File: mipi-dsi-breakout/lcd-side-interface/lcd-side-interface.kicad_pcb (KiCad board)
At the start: 2 copper layers, 8 parts

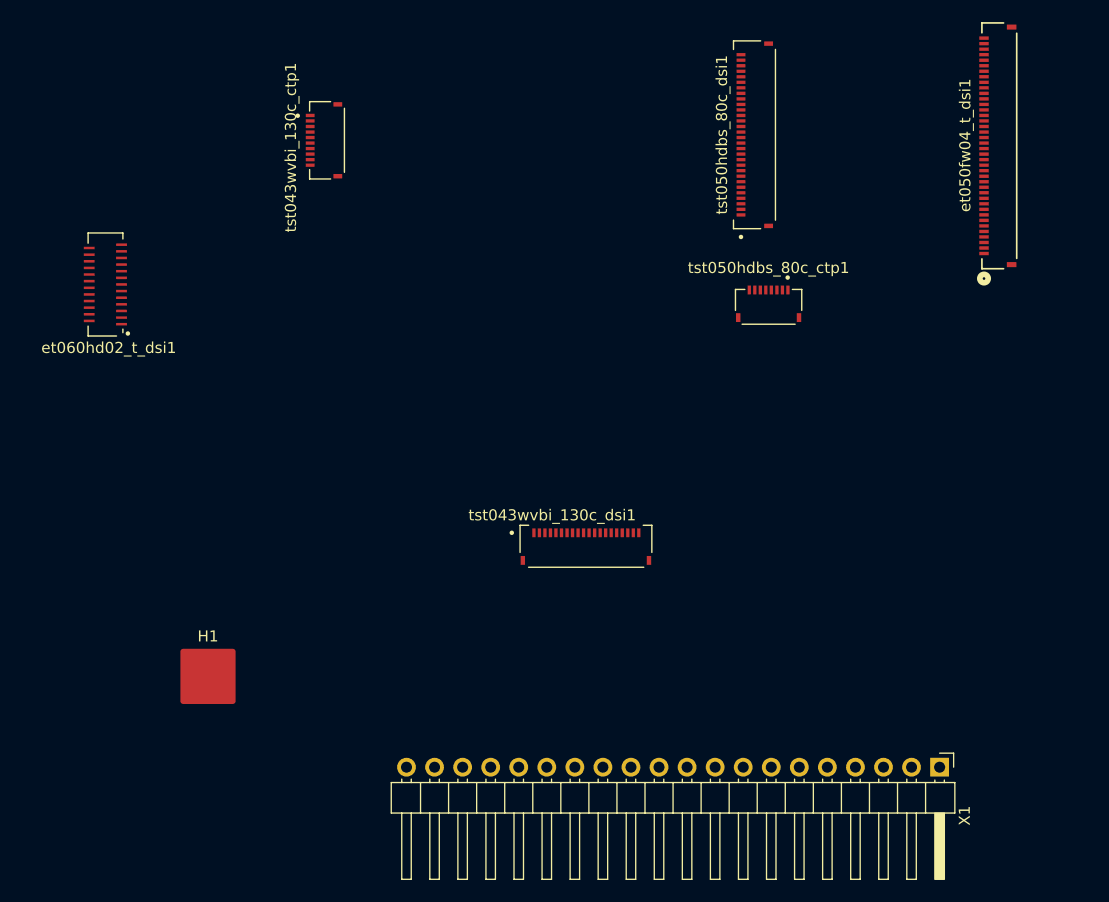
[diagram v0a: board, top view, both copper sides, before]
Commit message: Fill out lcd side interface + double check errors.
* Flip orientation of most connectors to match orientation of real world
  parts.

* Added NC pins to symbol so they are matched up to the footprints.

* Added a RESET_FAILSAFE solder bridge that can be cut in the case that
  the CTP touch screen resets aren't active low and the DSI resets are.

* Double check pin ordering and reset signals.
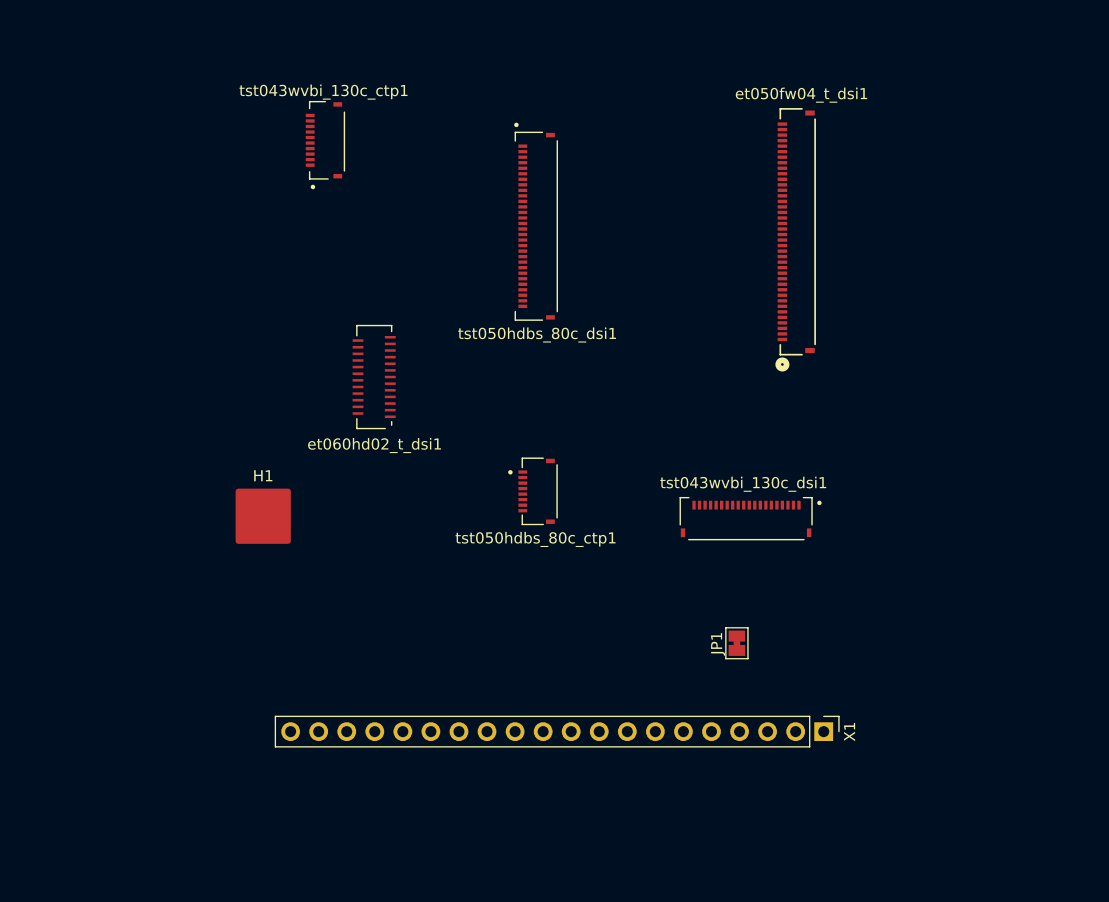
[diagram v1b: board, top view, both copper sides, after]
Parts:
- added JP1: SolderJumper_2_Bridged, Jumper:SolderJumper-2_P1.3mm_Bridged_Pad1.0x1.5mm, F.Cu at (153.9, 113.0)
- X1: footprint Connector_PinHeader_2.54mm:PinHeader_1x20_P2.54mm_Horizontal -> Connector_PinHeader_2.54mm:PinHeader_1x20_P2.54mm_Vertical
- moved tst050hdbs_80c_ctp1 27.1 mm to (135.7, 99.2), turned to 90 degrees
- moved et060hd02_t_dsi1 25.7 mm to (121.1, 89.2)
- moved tst050hdbs_80c_dsi1 21.4 mm to (135.7, 75.2)
- moved et050fw04_t_dsi1 19.8 mm to (158.0, 85.5)
- moved H1 15.3 mm to (111.0, 101.5)
- moved tst043wvbi_130c_dsi1 14.7 mm to (157.2, 101.7)
- moved X1 11.0 mm to (161.7, 121.0)
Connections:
- et050fw04_t_dsi1 pad 11: (no net) -> unconnected-(et050fw04_t_dsi1-NC-Pad11)
- et050fw04_t_dsi1 pad 12: (no net) -> unconnected-(et050fw04_t_dsi1-NC-Pad12)
- et050fw04_t_dsi1 pad 14: (no net) -> unconnected-(et050fw04_t_dsi1-NC-Pad14)
- et050fw04_t_dsi1 pad 15: (no net) -> unconnected-(et050fw04_t_dsi1-NC-Pad15)
- et050fw04_t_dsi1 pad 21: (no net) -> unconnected-(et050fw04_t_dsi1-NC-Pad21)
- et050fw04_t_dsi1 pad 23: (no net) -> unconnected-(et050fw04_t_dsi1-NC-Pad23)
- et050fw04_t_dsi1 pad 25: (no net) -> unconnected-(et050fw04_t_dsi1-NC-Pad25)
- et050fw04_t_dsi1 pad 26: (no net) -> unconnected-(et050fw04_t_dsi1-NC-Pad26)
- et050fw04_t_dsi1 pad 31: (no net) -> unconnected-(et050fw04_t_dsi1-NC-Pad31)
- et050fw04_t_dsi1 pad 34: (no net) -> unconnected-(et050fw04_t_dsi1-NC-Pad34)
- et050fw04_t_dsi1 pad 40: (no net) -> unconnected-(et050fw04_t_dsi1-NC-Pad40)
- et060hd02_t_dsi1 pad 20: (no net) -> unconnected-(et060hd02_t_dsi1-NC-Pad20)
- et060hd02_t_dsi1 pad 23: (no net) -> unconnected-(et060hd02_t_dsi1-NC-Pad23)
- tst043wvbi_130c_ctp1 pad 1: (no net) -> unconnected-(tst043wvbi_130c_ctp1-NC-Pad1)
- tst043wvbi_130c_ctp1 pad 2: (no net) -> unconnected-(tst043wvbi_130c_ctp1-NC-Pad2)
- tst043wvbi_130c_ctp1 pad 3: /RESET -> /RESET_FAILSAFE
- tst043wvbi_130c_dsi1 pad 20: (no net) -> GND
- tst050hdbs_80c_ctp1 pad 7: /RESET -> /RESET_FAILSAFE
- tst050hdbs_80c_dsi1 pad 1: (no net) -> unconnected-(tst050hdbs_80c_dsi1-NC-Pad1)
- tst050hdbs_80c_dsi1 pad 29: (no net) -> unconnected-(tst050hdbs_80c_dsi1-NC-Pad29)
- tst050hdbs_80c_dsi1 pad 30: (no net) -> unconnected-(tst050hdbs_80c_dsi1-NC-Pad30)
- tst050hdbs_80c_dsi1 pad 9: (no net) -> unconnected-(tst050hdbs_80c_dsi1-NC-Pad9)

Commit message: Do first pass of positioning for zif connectors.
In mipi dsi lcd side interface board. Need to double check measurements
again, just to be sure.
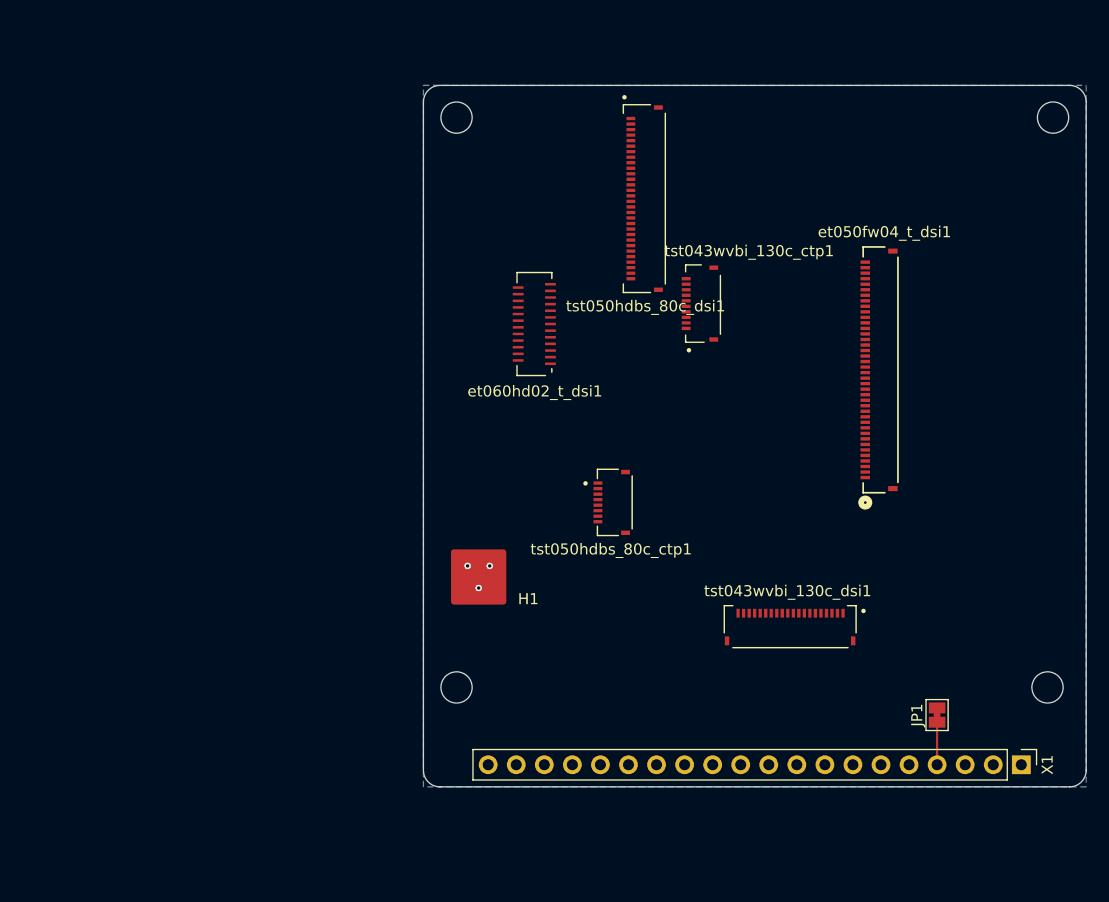
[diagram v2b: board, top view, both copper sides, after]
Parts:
- moved tst043wvbi_130c_ctp1 37.1 mm to (149.3, 80.0)
- moved H1 20.3 mm to (130.5, 107.0)
- moved JP1 19.3 mm to (172.0, 119.5)
- moved X1 18.1 mm to (179.6, 124.0)
- moved et060hd02_t_dsi1 15.3 mm to (135.6, 84.4)
- moved et050fw04_t_dsi1 14.6 mm to (165.5, 98.0)
- moved tst043wvbi_130c_dsi1 10.6 mm to (161.2, 111.5)
- moved tst050hdbs_80c_dsi1 10.1 mm to (145.5, 72.8)
- moved tst050hdbs_80c_ctp1 6.87 mm to (142.5, 100.2)
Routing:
- net /RESET: track 0.00 -> 3.85 mm
- net GND: vias 0 -> 3
- added copper zone on B.Cu, net GND
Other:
- board outline added: 60 x 63.5 mm
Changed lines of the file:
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@@
 	(footprint "Jumper:SolderJumper-2_P1.3mm_Bridged_Pad1.0x1.5mm"
 		(layer "F.Cu")
-		(at 153.88 113 90)
+		(at 172 119.5 90)
 		(descr "SMD Solder Jumper, 1x1.5mm Pads, 0.3mm gap, bridged with 1 copper strip")
 		(tags "net tie solder jumper bridged")
@@
 		)
 		(property "Value" "SolderJumper_2_Bridged"
-			(at 0 1.9 90)
+			(at 2.5 -0.3 0)
 			(layer "F.Fab")
 			(effects
@@
 	(footprint "project:sus-grounding-pad"
 		(layer "F.Cu")
-		(at 111 101.5)
+		(at 130.5 107)
 		(property "Reference" "H1"
-			(at 0 -3.625 0)
+			(at 4.5 2 0)
 			(unlocked yes)
 			(layer "F.SilkS")
@@
 		)
 		(property "Value" "MountingHole_Pad"
-			(at 0 3.625 0)
+			(at 0 4 0)
 			(unlocked yes)
 			(layer "F.Fab")
@@
 		)
 		(fp_text user "${REFERENCE}"
-			(at 0 5.625 0)
+			(at 4.5 2 0)
 			(unlocked yes)
 			(layer "F.Fab")
@@
 	(footprint "project:Cvilux_CF4240FH0R0-05-NH_40pos-0.5mm-zif"
 		(layer "F.Cu")
-		(at 158 85.500002 90)
+		(at 165.499878 98.000001 90)
 		(tags "CF4240FH0R0-05-NH ")
 		(property "Reference" "et050fw04_t_dsi1"
@@
 	(footprint "Connector_PinHeader_2.54mm:PinHeader_1x20_P2.54mm_Vertical"
 		(layer "F.Cu")
-		(at 161.74 121 -90)
+		(at 179.625 124 -90)
 		(descr "Through hole straight pin header, 1x20, 2.54mm pitch, single row")
 		(tags "Through hole pin header THT 1x20 2.54mm single row")
@@
 	(footprint "project:TE_2328702_8pos-0.5mm-zif"
 		(layer "F.Cu")
-		(at 135.7 99.25 90)
+		(at 142.5 100.25 90)
 		(property "Reference" "tst050hdbs_80c_ctp1"
 			(at -4.25 0 180)
@@
 	(footprint "project:Cvilux_CF4230FH0R0-05-NH_30pos-0.5mm-zif"
 		(layer "F.Cu")
-		(at 135.72 75.25 90)
+		(at 145.5 72.75 90)
 		(property "Reference" "tst050hdbs_80c_dsi1"
 			(at -9.741929 0.11858 0)
@@
 	(footprint "project:Cvilux_CF5825DH0RA-NH_25pos-0.3mm-zif"
 		(layer "F.Cu")
-		(at 121.1 89.19 90)
+		(at 135.6 84.39 90)
 		(property "Reference" "et060hd02_t_dsi1"
 			(at -5.81 0 0)
@@
 	(footprint "project:Cvilux_CF4220FH0R0-05-NH_20pos-0.5mm-zif"
 		(layer "F.Cu")
-		(at 157.25 101.72)
+		(at 161.2375 111.5)
 		(property "Reference" "tst043wvbi_130c_dsi1"
 			(at -2.75 -3.22 0)
@@
 	(footprint "project:TE_1-2328702-0_10pos-0.5mm-zif"
 		(layer "F.Cu")
-		(at 115.25 65.22 90)
+		(at 149.2875 80 90)
 		(property "Reference" "tst043wvbi_130c_ctp1"
-			(at 2.22 1.25 180)
+			(at 2.5 5.7125 180)
 			(layer "F.SilkS")
 			(effects
@@
 			)
 		)
+	)
+	(gr_line
+		(start 185.5 124.5)
+		(end 185.5 64)
+		(stroke
+			(width 0.05)
+			(type default)
+		)
+		(layer "Edge.Cuts")
+	)
+	(gr_circle
+		(center 182 117)
+		(end 183 118)
+		(stroke
+			(width 0.05)
+			(type default)
+		)
+		(fill no)
+		(layer "Edge.Cuts")
+	)
+	(gr_arc
+		(start 125.5 64)
+		(mid 125.93934 62.93934)
+		(end 127 62.5)
+		(stroke
+			(width 0.05)
+			(type default)
+		)
+		(layer "Edge.Cuts")
+	)
+	(gr_circle
+		(center 128.5 65.414214)
+		(end 129.5 66.414214)
+		(stroke
+			(width 0.05)
+			(type default)
+		)
+		(fill no)
+		(layer "Edge.Cuts")
+	)
+	(gr_line
+		(start 184 62.5)
+		(end 127 62.5)
+		(stroke
+			(width 0.05)
+			(type default)
+		)
+		(layer "Edge.Cuts")
+	)
+	(gr_line
+		(start 127 126)
+		(end 184 126)
+		(stroke
+			(width 0.05)
+			(type default)
+		)
+		(layer "Edge.Cuts")
+	)
+	(gr_arc
+		(start 127 126)
+		(mid 125.93934 125.56066)
+		(end 125.5 124.5)
+		(stroke
+			(width 0.05)
+			(type default)
+		)
+		(layer "Edge.Cuts")
+	)
+	(gr_circle
+		(center 128.5 117)
+		(end 129.5 118)
+		(stroke
+			(width 0.05)
+			(type default)
+		)
+		(fill no)
+		(layer "Edge.Cuts")
+	)
+	(gr_line
+		(start 125.5 64)
+		(end 125.5 124.5)
+		(stroke
+			(width 0.05)
+			(type default)
+		)
+		(layer "Edge.Cuts")
+	)
+	(gr_circle
+		(center 182.5 65.414214)
+		(end 183.5 66.414214)
+		(stroke
+			(width 0.05)
+			(type default)
+		)
+		(fill no)
+		(layer "Edge.Cuts")
+	)
+	(gr_arc
+		(start 185.5 124.5)
+		(mid 185.06066 125.56066)
+		(end 184 126)
+		(stroke
+			(width 0.05)
+			(type default)
+		)
+		(layer "Edge.Cuts")
+	)
+	(gr_arc
+		(start 184 62.5)
+		(mid 185.06066 62.93934)
+		(end 185.5 64)
+		(stroke
+			(width 0.05)
+			(type default)
+		)
+		(layer "Edge.Cuts")
+	)
+	(via
+		(at 129.5 106)
+		(size 0.6)
+		(drill 0.3)
+		(layers "F.Cu" "B.Cu")
+		(net 1)
+	)
+	(via
+		(at 131.5 106)
+		(size 0.6)
+		(drill 0.3)
+		(layers "F.Cu" "B.Cu")
+		(net 1)
+	)
+	(via
+		(at 130.5 108)
+		(size 0.6)
+		(drill 0.3)
+		(layers "F.Cu" "B.Cu")
+		(net 1)
+	)
+	(segment
+		(start 172 123.995)
+		(end 172.005 124)
+		(width 0.2)
+		(layer "F.Cu")
+		(net 6)
+	)
+	(segment
+		(start 172 120.15)
+		(end 172 123.995)
+		(width 0.2)
+		(layer "F.Cu")
+		(net 6)
+	)
+	(zone
+		(net 1)
+		(net_name "GND")
+		(layer "B.Cu")
+		(hatch edge 0.5)
+		(connect_pads
+			(clearance 0.5)
+		)
+		(min_thickness 0.25)
+		(filled_areas_thickness no)
+		(fill yes
+			(thermal_gap 0.5)
+			(thermal_bridge_width 0.5)
+		)
+		(polygon
+			(pts
+				(xy 125.5 62.5) (xy 185.5 62.5) (xy 185.5 126) (xy 125.5 126)
+			)
+		)
